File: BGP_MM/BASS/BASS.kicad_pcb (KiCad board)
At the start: 2 copper layers, 24 x 20.5 mm, 8 parts, among them J1 Conn_01x02_Male, J2 Conn_01x02_Male, J3 Conn_01x04_Male, J4 Conn_01x04_Male, P2 Conn_01x02, P3 Conn_01x02, P4 Conn_01x03

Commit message: Board Labels
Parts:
- moved J2 0.40 mm to (141.7, 98.8)
- moved J1 0.05 mm to (141.7, 93.4)
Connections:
- P2 pad 1: /JZ_I -> Earth
- P2 pad 2: Earth -> /JZ_I
- P3 pad 1: /MM_NH -> Earth
- P3 pad 2: Earth -> /MM_NH
- P4 pad 1: /MM_BH -> Earth
- P4 pad 3: Earth -> /MM_BH
- RV1 pad 1: Net-(J1-Pad1) -> Net-(RV1-Pad1)
- RV1 pad 2: Net-(J1-Pad2) -> Net-(J1-Pad1)
- RV1 pad 3: Net-(RV1-Pad3) -> Net-(J1-Pad2)
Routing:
- net /MM_BH: track 30.6 -> 24.7 mm
- net Net-(J1-Pad1): track 13.6 -> 10.6 mm
- net Net-(J1-Pad2): track 11.5 -> 9.40 mm
- net /JZ_I: track 14.6 -> 15.7 mm
- net /MM_NH: track 22.9 -> 23.9 mm
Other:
- board size 24 x 20.5 mm -> 24 x 21 mm
- board text added: "BC"
- board text added: "BH"
- board text added: "EA"
- board text added: "JC"
- board text added: "JH"
- board text added: "MM Sabre Bass/Mixer CBD Design"
- board text added: "MMS"
- board text added: "NC"
- board text added: "NH"
- board text added: "SEL"
- board text added: "TRB"
- board text added: "VOL"

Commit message: MM Gerbers, BASS pot fixup
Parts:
- moved RV1 0.50 mm to (137.5, 85.0)
- moved P3 0.36 mm to (149.8, 91.1)
- moved P2 0.36 mm to (149.8, 96.9)
- moved P4 0.36 mm to (149.8, 82.8)
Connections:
- RV1 pad 1: Net-(RV1-Pad1) -> Net-(J1-Pad1)
- RV1 pad 2: Net-(J1-Pad1) -> Net-(J1-Pad2)
- RV1 pad 3: Net-(J1-Pad2) -> Net-(RV1-Pad3)
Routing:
- net Net-(J1-Pad1): track 10.6 -> 12.7 mm
- net Net-(J1-Pad2): track 9.40 -> 11.0 mm
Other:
- board size 24 x 21 mm -> 24 x 20 mm

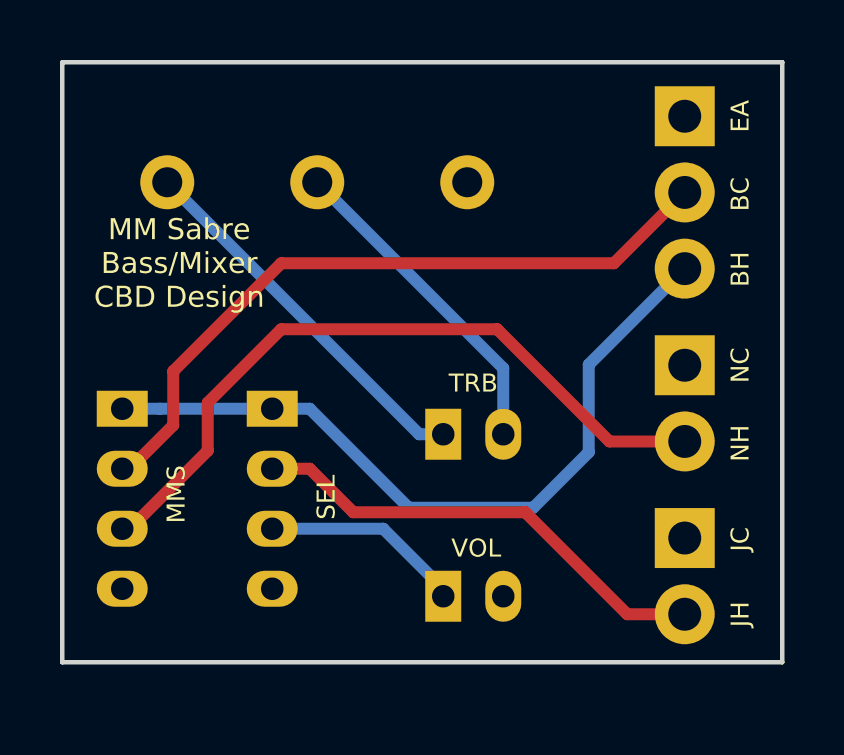
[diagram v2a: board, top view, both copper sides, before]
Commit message: MM Switch Config Changed
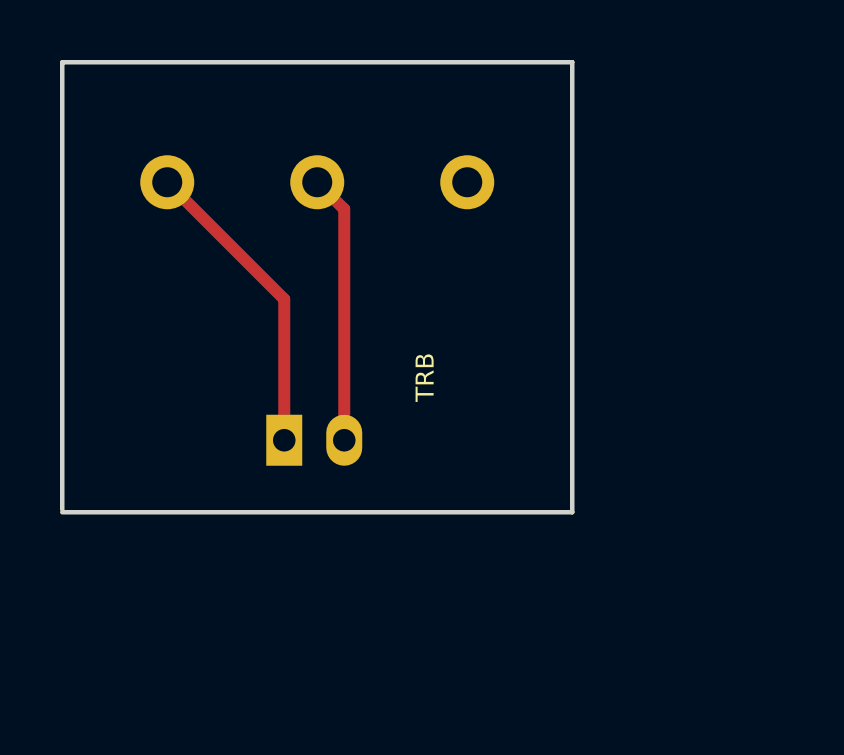
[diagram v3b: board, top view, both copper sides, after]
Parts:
- removed J2: Conn_01x02_Male, Connectors_JST:JST_PH_B2B-PH-K_02x2.00mm_Straight
- removed J3, J4: Conn_01x04_Male, Connectors_JST:JST_PH_B4B-PH-K_04x2.00mm_Straight
- removed P2, P3: Conn_01x02, Terminal_Blocks:TerminalBlock_Pheonix_MPT-2.54mm_2pol
- removed P4: Conn_01x03, Terminal_Blocks:TerminalBlock_Pheonix_MPT-2.54mm_3pol
- moved J1 5.30 mm to (136.4, 93.6)
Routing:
- net /MM_BH: track 25.1 -> 0.00 mm
- net /MM_NH: track 24.0 -> 0.00 mm
- net /MM_BC: track 23.6 -> 0.00 mm
- net /JZ_I: track 15.8 -> 0.00 mm
- net /SIG_O: track 7.03 -> 0.00 mm
- net Net-(J1-Pad1): track 12.7 -> 10.2 mm
- net Net-(J1-Pad2): track 11.0 -> 8.97 mm
- added copper zone on B.Cu, net (none)
- added copper zone on F.Cu, net (none)
- removed copper zone on B.Cu, net Earth
- removed copper zone on F.Cu, net Earth
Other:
- board size 24 x 20 mm -> 17 x 15 mm
- board text removed: "BC"
- board text removed: "BH"
- board text removed: "EA"
- board text removed: "JC"
- board text removed: "JH"
- board text removed: "MMS"
- board text removed: "NC"
- board text removed: "NH"
- board text removed: "SEL"
- board text removed: "VOL"

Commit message: MM Refactoring
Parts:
- J1: footprint Connectors_JST:JST_PH_B2B-PH-K_02x2.00mm_Straight -> Pin_Headers:Pin_Header_Straight_2x01_Pitch2.54mm
- moved J1 3.95 mm to (132.5, 93.0)
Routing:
- net Net-(J1-Pad1): track 10.2 -> 8.00 mm
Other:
- board text removed: "MM Sabre Bass/Mixer CBD Design"
- board text removed: "TRB"
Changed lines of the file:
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@@
   (general
     (links 2)
-    (no_connects 0)
+    (no_connects 2)
     (area 128.924999 80.924999 146.075001 96.075001)
     (thickness 1.6)
-    (drawings 10)
+    (drawings 8)
     (tracks 4)
     (zones 0)
@@
     )
   )
-  (module Connectors_JST:JST_PH_B2B-PH-K_02x2.00mm_Straight (layer B.Cu)
-    (at 136.4 93.6)
-    (descr "JST PH series connector, B2B-PH-K, top entry type, through hole, Datasheet: http://www.jst-mfg.com/product/pdf/eng/ePH.pdf")
-    (tags "connector jst ph")
-    (fp_text reference J1 (at 1 -1.5) (layer B.SilkS)
+  (module Pin_Headers:Pin_Header_Straight_2x01_Pitch2.54mm (layer B.Cu)
+    (at 132.5 93)
+    (descr "Through hole straight pin header, 2x01, 2.54mm pitch, double rows")
+    (tags "Through hole pin header THT 2x01 2.54mm double row")
+    (fp_text reference J1 (at 1.27 2.33) (layer B.SilkS)
       (effects (font (size 0.7 0.7) (thickness 0.15)) (justify mirror))
     )
-    (fp_text value Conn_01x02_Male (at 1 -3.8) (layer B.Fab) hide
+    (fp_text value Conn_01x02_Male (at 1.27 -2.33) (layer B.Fab) hide
       (effects (font (size 0.7 0.7) (thickness 0.15)) (justify mirror))
     )
-    (fp_line (start -2.05 1.8) (end -2.05 -2.9) (layer B.SilkS) (width 0.12))
-    (fp_line (start -2.05 -2.9) (end 4.05 -2.9) (layer B.SilkS) (width 0.12))
-    (fp_line (start 4.05 -2.9) (end 4.05 1.8) (layer B.SilkS) (width 0.12))
-    (fp_line (start 4.05 1.8) (end -2.05 1.8) (layer B.SilkS) (width 0.12))
-    (fp_line (start 0.5 1.8) (end 0.5 1.2) (layer B.SilkS) (width 0.12))
-    (fp_line (start 0.5 1.2) (end -1.45 1.2) (layer B.SilkS) (width 0.12))
-    (fp_line (start -1.45 1.2) (end -1.45 -2.3) (layer B.SilkS) (width 0.12))
-    (fp_line (start -1.45 -2.3) (end 3.45 -2.3) (layer B.SilkS) (width 0.12))
-    (fp_line (start 3.45 -2.3) (end 3.45 1.2) (layer B.SilkS) (width 0.12))
-    (fp_line (start 3.45 1.2) (end 1.5 1.2) (layer B.SilkS) (width 0.12))
-    (fp_line (start 1.5 1.2) (end 1.5 1.8) (layer B.SilkS) (width 0.12))
-    (fp_line (start -2.05 0.5) (end -1.45 0.5) (layer B.SilkS) (width 0.12))
-    (fp_line (start -2.05 -0.8) (end -1.45 -0.8) (layer B.SilkS) (width 0.12))
-    (fp_line (start 4.05 0.5) (end 3.45 0.5) (layer B.SilkS) (width 0.12))
-    (fp_line (start 4.05 -0.8) (end 3.45 -0.8) (layer B.SilkS) (width 0.12))
-    (fp_line (start -0.3 1.8) (end -0.3 2) (layer B.SilkS) (width 0.12))
-    (fp_line (start -0.3 2) (end -0.6 2) (layer B.SilkS) (width 0.12))
-    (fp_line (start -0.6 2) (end -0.6 1.8) (layer B.SilkS) (width 0.12))
-    (fp_line (start -0.3 1.9) (end -0.6 1.9) (layer B.SilkS) (width 0.12))
-    (fp_line (start 0.9 -2.3) (end 0.9 -1.8) (layer B.SilkS) (width 0.12))
-    (fp_line (start 0.9 -1.8) (end 1.1 -1.8) (layer B.SilkS) (width 0.12))
-    (fp_line (start 1.1 -1.8) (end 1.1 -2.3) (layer B.SilkS) (width 0.12))
-    (fp_line (start 1 -2.3) (end 1 -1.8) (layer B.SilkS) (width 0.12))
-    (fp_line (start -1.1 2.1) (end -2.35 2.1) (layer B.SilkS) (width 0.12))
-    (fp_line (start -2.35 2.1) (end -2.35 0.85) (layer B.SilkS) (width 0.12))
-    (fp_line (start -1.1 2.1) (end -2.35 2.1) (layer B.Fab) (width 0.1))
-    (fp_line (start -2.35 2.1) (end -2.35 0.85) (layer B.Fab) (width 0.1))
-    (fp_line (start -1.95 1.7) (end -1.95 -2.8) (layer B.Fab) (width 0.1))
-    (fp_line (start -1.95 -2.8) (end 3.95 -2.8) (layer B.Fab) (width 0.1))
-    (fp_line (start 3.95 -2.8) (end 3.95 1.7) (layer B.Fab) (width 0.1))
-    (fp_line (start 3.95 1.7) (end -1.95 1.7) (layer B.Fab) (width 0.1))
-    (fp_line (start -2.45 2.2) (end -2.45 -3.3) (layer B.CrtYd) (width 0.05))
-    (fp_line (start -2.45 -3.3) (end 4.45 -3.3) (layer B.CrtYd) (width 0.05))
-    (fp_line (start 4.45 -3.3) (end 4.45 2.2) (layer B.CrtYd) (width 0.05))
-    (fp_line (start 4.45 2.2) (end -2.45 2.2) (layer B.CrtYd) (width 0.05))
-    (fp_text user %R (at 1 -1.5) (layer B.Fab) hide
+    (fp_line (start 0 1.27) (end 3.81 1.27) (layer B.Fab) (width 0.1))
+    (fp_line (start 3.81 1.27) (end 3.81 -1.27) (layer B.Fab) (width 0.1))
+    (fp_line (start 3.81 -1.27) (end -1.27 -1.27) (layer B.Fab) (width 0.1))
+    (fp_line (start -1.27 -1.27) (end -1.27 0) (layer B.Fab) (width 0.1))
+    (fp_line (start -1.27 0) (end 0 1.27) (layer B.Fab) (width 0.1))
+    (fp_line (start -1.33 -1.33) (end 3.87 -1.33) (layer B.SilkS) (width 0.12))
+    (fp_line (start -1.33 -1.27) (end -1.33 -1.33) (layer B.SilkS) (width 0.12))
+    (fp_line (start 3.87 1.33) (end 3.87 -1.33) (layer B.SilkS) (width 0.12))
+    (fp_line (start -1.33 -1.27) (end 1.27 -1.27) (layer B.SilkS) (width 0.12))
+    (fp_line (start 1.27 -1.27) (end 1.27 1.33) (layer B.SilkS) (width 0.12))
+    (fp_line (start 1.27 1.33) (end 3.87 1.33) (layer B.SilkS) (width 0.12))
+    (fp_line (start -1.33 0) (end -1.33 1.33) (layer B.SilkS) (width 0.12))
+    (fp_line (start -1.33 1.33) (end 0 1.33) (layer B.SilkS) (width 0.12))
+    (fp_line (start -1.8 1.8) (end -1.8 -1.8) (layer B.CrtYd) (width 0.05))
+    (fp_line (start -1.8 -1.8) (end 4.35 -1.8) (layer B.CrtYd) (width 0.05))
+    (fp_line (start 4.35 -1.8) (end 4.35 1.8) (layer B.CrtYd) (width 0.05))
+    (fp_line (start 4.35 1.8) (end -1.8 1.8) (layer B.CrtYd) (width 0.05))
+    (fp_text user %R (at 1.27 0 270) (layer B.Fab) hide
       (effects (font (size 0.7 0.7) (thickness 0.15)) (justify mirror))
     )
-    (pad 1 thru_hole rect (at 0 0) (size 1.2 1.7) (drill 0.75) (layers *.Cu *.Mask)
+    (pad 1 thru_hole rect (at 0 0) (size 1.7 1.7) (drill 1) (layers *.Cu *.Mask)
       (net 1 "Net-(J1-Pad1)"))
-    (pad 2 thru_hole oval (at 2 0) (size 1.2 1.7) (drill 0.75) (layers *.Cu *.Mask)
+    (pad 2 thru_hole oval (at 2.54 0) (size 1.7 1.7) (drill 1) (layers *.Cu *.Mask)
       (net 2 "Net-(J1-Pad2)"))
-    (model ${KISYS3DMOD}/Connectors_JST.3dshapes/JST_PH_B2B-PH-K_02x2.00mm_Straight.wrl
+    (model ${KISYS3DMOD}/Pin_Headers.3dshapes/Pin_Header_Straight_2x01_Pitch2.54mm.wrl
       (at (xyz 0 0 0))
       (scale (xyz 1 1 1))
       (rotate (xyz 0 0 0))
     )
-  )
-  (gr_text "MM Sabre\nBass/Mixer\nCBD Design" (at 142.7 92.1) (layer B.SilkS)
-    (effects (font (size 0.7 0.7) (thickness 0.175)) (justify mirror))
-  )
-  (gr_text TRB (at 141.1 91.5 90) (layer F.SilkS)
-    (effects (font (size 0.6 0.6) (thickness 0.15)))
   )
   (gr_line (start 129.3 95.7) (end 145.7 95.7) (layer Margin) (width 0.2))
@@
   (gr_line (start 129 81) (end 129 95.9) (layer Edge.Cuts) (width 0.15))
   (gr_line (start 146 81) (end 129 81) (layer Edge.Cuts) (width 0.15))
-  (segment (start 136.4 93.6) (end 136.4 88.9) (width 0.4) (layer F.Cu) (net 1))
-  (segment (start 136.4 88.9) (end 132.5 85) (width 0.4) (layer F.Cu) (net 1))
-  (segment (start 138.4 93.6) (end 138.4 85.9) (width 0.4) (layer F.Cu) (net 2))
-  (segment (start 138.4 85.9) (end 137.5 85) (width 0.4) (layer F.Cu) (net 2))
+  (segment (start 132.5 93) (end 132.5 85) (width 0.4) (layer F.Cu) (net 1))
+  (segment (start 135.04 93) (end 135.1 93) (width 0.4) (layer F.Cu) (net 2))
+  (segment (start 135.1 93) (end 137.5 90.6) (width 0.4) (layer F.Cu) (net 2))
+  (segment (start 137.5 90.6) (end 137.5 85) (width 0.4) (layer F.Cu) (net 2))
   (zone (net 0) (net_name "") (layer F.Cu) (hatch edge 0.508)
     (connect_pads (clearance 0.3))

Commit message: Minor tweaks for MM/F0 - gerbers ready to go out
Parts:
- moved J1 3.70 mm to (136.2, 93.0)
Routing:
- net Net-(J1-Pad1): track 8.00 -> 9.53 mm
- net Net-(J1-Pad2): track 9.05 -> 8.51 mm
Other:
- net class Default: clearance 0.3 -> 0.5
- net class PWR: clearance 0.3 -> 0.5
- rule trace_clearance: 0.3 -> 0.5
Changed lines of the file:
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@@
   (setup
     (last_trace_width 0.4)
-    (trace_clearance 0.3)
-    (zone_clearance 0.25)
+    (trace_clearance 0.5)
+    (zone_clearance 0.5)
     (zone_45_only no)
     (trace_min 0.3)
@@
   (net 3 "Net-(RV1-Pad3)")
   (net_class Default "This is the default net class."
-    (clearance 0.3)
+    (clearance 0.5)
     (trace_width 0.4)
     (via_dia 0.6)
@@
   )
   (net_class PWR ""
-    (clearance 0.3)
+    (clearance 0.5)
     (trace_width 0.6)
     (via_dia 0.6)
@@
   )
   (module Pin_Headers:Pin_Header_Straight_2x01_Pitch2.54mm (layer B.Cu)
-    (at 132.5 93)
+    (at 136.2 93)
     (descr "Through hole straight pin header, 2x01, 2.54mm pitch, double rows")
     (tags "Through hole pin header THT 2x01 2.54mm double row")
@@
   (gr_line (start 129 81) (end 129 95.9) (layer Edge.Cuts) (width 0.15))
   (gr_line (start 146 81) (end 129 81) (layer Edge.Cuts) (width 0.15))
-  (segment (start 132.5 93) (end 132.5 85) (width 0.4) (layer F.Cu) (net 1))
-  (segment (start 135.04 93) (end 135.1 93) (width 0.4) (layer F.Cu) (net 2))
-  (segment (start 135.1 93) (end 137.5 90.6) (width 0.4) (layer F.Cu) (net 2))
-  (segment (start 137.5 90.6) (end 137.5 85) (width 0.4) (layer F.Cu) (net 2))
+  (segment (start 136.2 93) (end 136.2 88.7) (width 0.75) (layer F.Cu) (net 1))
+  (segment (start 136.2 88.7) (end 132.5 85) (width 0.75) (layer F.Cu) (net 1))
+  (segment (start 138.74 93) (end 138.74 86.24) (width 0.75) (layer F.Cu) (net 2))
+  (segment (start 138.74 86.24) (end 137.5 85) (width 0.75) (layer F.Cu) (net 2))
   (zone (net 0) (net_name "") (layer F.Cu) (hatch edge 0.508)
-    (connect_pads (clearance 0.25))
-    (min_thickness 0.25)
-    (fill yes (arc_segments 32) (thermal_gap 0.25) (thermal_bridge_width 0.6))
+    (connect_pads (clearance 0.5))
+    (min_thickness 0.5)
+    (fill yes (arc_segments 32) (thermal_gap 0.5) (thermal_bridge_width 0.6))
     (polygon
       (pts

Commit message: Gerbers altered and sent
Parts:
- moved J1 0.90 mm to (136.2, 92.1)
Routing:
- net Net-(J1-Pad1): track 9.53 -> 8.63 mm
- net Net-(J1-Pad2): track 8.51 -> 7.61 mm
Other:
- board size 17 x 15 mm -> 17 x 13 mm
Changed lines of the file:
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@@
-(kicad_pcb (version 4) (host pcbnew 4.0.4-1.fc24-product)
+(kicad_pcb (version 4) (host pcbnew 4.0.7)
   (general
     (links 2)
     (no_connects 0)
-    (area 127.135 80.624999 146.575001 96.265)
+    (area 126.935 80.424999 146.775001 96.465)
     (thickness 1.6)
     (drawings 8)
@@
   )
   (module Pin_Headers:Pin_Header_Straight_2x01_Pitch2.54mm (layer B.Cu)
-    (at 136.2 93)
+    (at 136.2 92.1)
     (descr "Through hole straight pin header, 2x01, 2.54mm pitch, double rows")
     (tags "Through hole pin header THT 2x01 2.54mm double row")
@@
     )
   )
-  (gr_line (start 129.3 95.7) (end 145.7 95.7) (layer Margin) (width 0.2))
-  (gr_line (start 145.7 95.7) (end 145.7 81.3) (layer Margin) (width 0.2))
-  (gr_line (start 129.3 81.3) (end 129.3 95.7) (layer Margin) (width 0.2))
+  (gr_line (start 129.3 93.7) (end 145.7 93.7) (layer Margin) (width 0.2))
+  (gr_line (start 145.7 93.7) (end 145.7 81.3) (layer Margin) (width 0.2))
+  (gr_line (start 129.3 81.3) (end 129.3 93.7) (layer Margin) (width 0.2))
   (gr_line (start 145.7 81.3) (end 129.3 81.3) (layer Margin) (width 0.2))
-  (gr_line (start 146 96) (end 146 81) (layer Edge.Cuts) (width 0.15))
-  (gr_line (start 129 96) (end 146 96) (layer Edge.Cuts) (width 0.15))
-  (gr_line (start 129 81) (end 129 95.9) (layer Edge.Cuts) (width 0.15))
+  (gr_line (start 146 94) (end 146 81) (layer Edge.Cuts) (width 0.15))
+  (gr_line (start 129 94) (end 146 94) (layer Edge.Cuts) (width 0.15))
+  (gr_line (start 129 81) (end 129 94) (layer Edge.Cuts) (width 0.15))
   (gr_line (start 146 81) (end 129 81) (layer Edge.Cuts) (width 0.15))
-  (segment (start 136.2 93) (end 136.2 88.7) (width 0.75) (layer F.Cu) (net 1))
+  (segment (start 136.2 88.7) (end 136.2 92.1) (width 0.75) (layer F.Cu) (net 1))
   (segment (start 136.2 88.7) (end 132.5 85) (width 0.75) (layer F.Cu) (net 1))
-  (segment (start 138.74 93) (end 138.74 86.24) (width 0.75) (layer F.Cu) (net 2))
+  (segment (start 138.74 86.24) (end 138.74 92.1) (width 0.75) (layer F.Cu) (net 2))
   (segment (start 138.74 86.24) (end 137.5 85) (width 0.75) (layer F.Cu) (net 2))
   (zone (net 0) (net_name "") (layer F.Cu) (hatch edge 0.508)
@@
     (polygon
       (pts
-        (xy 146 81) (xy 129 81) (xy 129 96) (xy 146 96)
+        (xy 146 81) (xy 129 81) (xy 129 94) (xy 146 94)
       )
     )
@@
     (polygon
       (pts
-        (xy 146 81) (xy 129 81) (xy 129 96) (xy 146 96)
+        (xy 146 81) (xy 129 81) (xy 129 94) (xy 146 94)
       )
     )
